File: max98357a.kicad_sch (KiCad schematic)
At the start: 1 part, among them U6 MAX98357A

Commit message: ESP32S3 branch initial changes
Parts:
- added C28: 100nf, Capacitor_SMD:C_0805_2012Metric, symbol Device:C
- added C30: 22p, Capacitor_SMD:C_0805_2012Metric, symbol Device:C
- added C37: 220p, Capacitor_SMD:C_0805_2012Metric, symbol Device:C
- added C38: 10uf, Capacitor_SMD:C_0805_2012Metric, symbol Device:C
- added L1, L3: ferrite, symbol Device:L
- added L4, L5: ferrite, Inductor_SMD:L_0805_2012Metric, symbol Device:L
- added LS1: Speaker, symbol Device:Speaker
- added R36: 1M, Resistor_SMD:R_0805_2012Metric, symbol Device:R
- added R37: 0, Jumper:SolderJumper-2_P1.3mm_Open_RoundedPad1.0x1.5mm, symbol Device:R
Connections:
- net DIN: now reaches U6.1 (DIN)
- net OUTN: now reaches U6.10 (OUTN)
- net OUTN: now also L1.1
- net GNDA: now reaches U6.11 (GND), U6.15 (GND), U6.3 (GND)
- net GNDA: now also C28.1, C30.1, C37.1, C38.1, R37.1
- net LRC: now reaches U6.14 (LRCLK)
- net BCLK: now reaches U6.16 (BCLK)
- net pad: now reaches U6.17 (PAD)
- net GAIN: now reaches U6.2 (GAIN_SLOT)
- net SD: now reaches U6.4 (~{SD_MODE})
- net SD: now also R36.2
- net at U6.7 (VDD), U6.8 (VDD): now also C28.2, C38.2, L4.1, L5.1
- net OUTP: now reaches U6.9 (OUTP)
- net OUTP: now also L3.1
- new net: C30.2, L3.2, LS1.1
- new net: C37.2, L1.2, LS1.2
- new net +3V3: L4.2, R36.1
- new net +5V: L5.2
- new net GND: R37.2

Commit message: Update KiCad project files
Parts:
- added J7: Conn_01x07_Pin, Connector_PinHeader_2.54mm:PinHeader_1x07_P2.54mm_Vertical, symbol Connector:Conn_01x07_Pin
- LS1: footprint (none) -> Connector_Molex:Molex_Micro-Latch_53253-0270_1x02_P2.00mm_Vertical
- renumbered C28 to C20, C38 to C21, C37 to C22, C30 to C23, L4 to L3, L5 to L4, L1 to L5, L3 to L6, R36 to R25, R37 to R26, U6 to U5
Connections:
- net BCLK: now also J7.5 (Pin_5)
- net DIN: now also J7.6 (Pin_6)
- net GAIN: now also J7.1 (Pin_1)
- net GNDA: now also J7.7 (Pin_7)
- net LRC: now also J7.4 (Pin_4)
- net SD: now also J7.2 (Pin_2)
- net at C20.2, C21.2, L3.1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: now also J7.3 (Pin_3)
- net pad renamed PAD
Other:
- moved on the sheet: C22, L5, L6

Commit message: Remove unused schematic files, lock files, and backup directories
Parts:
- removed R26: 0, Jumper:SolderJumper-2_P1.3mm_Open_RoundedPad1.0x1.5mm, symbol Device:R
- added JP7: 0, Jumper:SolderJumper-2_P1.3mm_Open_RoundedPad1.0x1.5mm, symbol Jumper:Jumper_2_Open
- J7: value Conn_01x07_Pin -> (none)
- L5, L6: footprint (none) -> Inductor_SMD:L_0805_2012Metric
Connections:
- net BCLK: now also J7.2 (Pin_2); no longer J7.5 (Pin_5)
- net DIN: now also J7.3 (Pin_3); no longer J7.6 (Pin_6)
- net GAIN: now also J7.4 (Pin_4); no longer J7.1 (Pin_1)
- net GND: now also JP7.1 (A)
- net GNDA: now also J7.6 (Pin_6), JP7.2 (B); no longer J7.7 (Pin_7)
- net LRC: now also J7.1 (Pin_1); no longer J7.4 (Pin_4)
- net SD: now also J7.5 (Pin_5); no longer J7.2 (Pin_2)
- net VCC_MAC98357: now reaches C20.2, C21.2, L3.1, L4.1, U5.7 (VDD), U5.8 (VDD)
- net VCC_MAC98357: now also J7.7 (Pin_7); no longer J7.3 (Pin_3)
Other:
- moved on the sheet: J7, R25

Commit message: Update all schematic files and project
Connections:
- net VCC_MAC98357 renamed VCC_MAX98357
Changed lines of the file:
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@@
 		)
 	)
-	(label "VCC_MAC98357"
+	(label "VCC_MAX98357"
 		(at 148.59 86.36 0)
 		(effects
@@
 		)
 	)
-	(label "VCC_MAC98357"
+	(label "VCC_MAX98357"
 		(at 90.17 109.22 0)
 		(effects

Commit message: Update all schematic files and project
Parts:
- added R65, R66: 100k, Resistor_SMD:R_0805_2012Metric, symbol Device:R
- added R67: 68k, Resistor_SMD:R_0805_2012Metric, symbol Device:R
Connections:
- net PAD is gone; now on net GNDA: U5.17 (PAD)
- net GAIN: now also R65.1, R66.2
- net GNDA: now also R65.2
- net SD: now also R67.1; no longer U5.4 (~{SD_MODE})
- net VCC_MAX98357: now also R66.1
- new net: R67.2, U5.4 (~{SD_MODE})
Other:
- moved on the sheet: J7

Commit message: Update schematics, PCB, and project files
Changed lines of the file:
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@@
+	)
+	(junction
+		(at 160.02 85.09)
+		(diameter 0)
+		(color 0 0 0 0)
 	)
 	(junction
@@
 	(wire
 		(pts
+			(xy 76.2 80.01) (xy 76.2 82.55)
+		)
+		(stroke
+			(width 0)
+			(type default)
+		)
+	)
+	(wire
+		(pts
 			(xy 59.69 95.25) (xy 68.58 95.25)
 		)
@@
 	(wire
 		(pts
+			(xy 116.84 101.6) (xy 119.38 101.6)
+		)
+		(stroke
+			(width 0)
+			(type default)
+		)
+	)
+	(wire
+		(pts
+			(xy 160.02 76.2) (xy 160.02 85.09)
+		)
+		(stroke
+			(width 0)
+			(type default)
+		)
+	)
+	(wire
+		(pts
 			(xy 147.32 114.3) (xy 152.4 114.3)
 		)
@@
 	(wire
 		(pts
+			(xy 160.02 86.36) (xy 173.99 86.36)
+		)
+		(stroke
+			(width 0)
+			(type default)
+		)
+	)
+	(wire
+		(pts
 			(xy 142.24 116.84) (xy 142.24 111.76)
 		)
@@
 	(wire
 		(pts
+			(xy 160.02 86.36) (xy 160.02 85.09)
+		)
+		(stroke
+			(width 0)
+			(type default)
+		)
+	)
+	(wire
+		(pts
 			(xy 218.44 106.68) (xy 218.44 113.03)
 		)
@@
 	(wire
 		(pts
-			(xy 81.28 90.17) (xy 76.2 90.17)
-		)
-		(stroke
-			(width 0)
-			(type default)
-		)
-	)
-	(wire
-		(pts
 			(xy 118.11 91.44) (xy 132.08 91.44)
 		)
@@
 	(wire
 		(pts
-			(xy 144.78 86.36) (xy 173.99 86.36)
+			(xy 144.78 85.09) (xy 160.02 85.09)
 		)
 		(stroke
@@
 	(wire
 		(pts
-			(xy 118.11 101.6) (xy 119.38 101.6)
+			(xy 144.78 85.09) (xy 144.78 86.36)
 		)
 		(stroke
@@
 	(wire
 		(pts
-			(xy 76.2 78.74) (xy 76.2 82.55)
-		)
-		(stroke
-			(width 0)
-			(type default)
-		)
-	)
-	(wire
-		(pts
 			(xy 217.17 106.68) (xy 218.44 106.68)
 		)
@@
 		(pts
 			(xy 76.2 100.33) (xy 76.2 102.87)
+		)
+		(stroke
+			(width 0)
+			(type default)
+		)
+	)
+	(wire
+		(pts
+			(xy 82.55 80.01) (xy 76.2 80.01)
+		)
+		(stroke
+			(width 0)
+			(type default)
+		)
+	)
+	(wire
+		(pts
+			(xy 88.9 90.17) (xy 76.2 90.17)
 		)
 		(stroke
@@
 	)
 	(label "VCC_MAX98357"
-		(at 148.59 86.36 0)
-		(effects
-			(font
-				(size 1.27 1.27)
-			)
-			(justify left bottom)
-		)
-	)
-	(label "VCC_MAX98357"
 		(at 59.69 104.14 0)
 		(effects
@@
 		)
 	)
-	(label "VCC_MAX98357"
-		(at 76.2 78.74 0)
-		(effects
-			(font
-				(size 1.27 1.27)
-			)
-			(justify left bottom)
+	(global_label "VCC_MAX98357"
+		(shape input)
+		(at 82.55 80.01 0)
+		(fields_autoplaced yes)
+		(effects
+			(font
+				(size 1.27 1.27)
+			)
+			(justify left)
+		)
+		(property "Intersheetrefs" "${INTERSHEET_REFS}"
+			(at 99.9284 80.01 0)
+			(hide yes)
+			(show_name no)
+			(do_not_autoplace no)
+			(effects
+				(font
+					(size 1.27 1.27)
+				)
+				(justify left)
+			)
+		)
+	)
+	(global_label "GAIN"
+		(shape input)
+		(at 118.11 104.14 180)
+		(fields_autoplaced yes)
+		(effects
+			(font
+				(size 1.27 1.27)
+			)
+			(justify right)
+		)
+		(property "Intersheetrefs" "${INTERSHEET_REFS}"
+			(at 110.8309 104.14 0)
+			(hide yes)
+			(show_name no)
+			(do_not_autoplace no)
+			(effects
+				(font
+					(size 1.27 1.27)
+				)
+				(justify right)
+			)
+		)
+	)
+	(global_label "VCC_MAX98357"
+		(shape input)
+		(at 160.02 76.2 180)
+		(fields_autoplaced yes)
+		(effects
+			(font
+				(size 1.27 1.27)
+			)
+			(justify right)
+		)
+		(property "Intersheetrefs" "${INTERSHEET_REFS}"
+			(at 142.6416 76.2 0)
+			(hide yes)
+			(show_name no)
+			(do_not_autoplace no)
+			(effects
+				(font
+					(size 1.27 1.27)
+				)
+				(justify right)
+			)
+		)
+	)
+	(global_label "SD"
+		(shape input)
+		(at 74.93 139.7 180)
+		(fields_autoplaced yes)
+		(effects
+			(font
+				(size 1.27 1.27)
+			)
+			(justify right)
+		)
+		(property "Intersheetrefs" "${INTERSHEET_REFS}"
+			(at 69.4653 139.7 0)
+			(hide yes)
+			(show_name no)
+			(do_not_autoplace no)
+			(effects
+				(font
+					(size 1.27 1.27)
+				)
+				(justify right)
+			)
+		)
+	)
+	(global_label "SD"
+		(shape input)
+		(at 59.69 92.71 0)
+		(fields_autoplaced yes)
+		(effects
+			(font
+				(size 1.27 1.27)
+			)
+			(justify left)
+		)
+		(property "Intersheetrefs" "${INTERSHEET_REFS}"
+			(at 65.1547 92.71 0)
+			(hide yes)
+			(show_name no)
+			(do_not_autoplace no)
+			(effects
+				(font
+					(size 1.27 1.27)
+				)
+				(justify left)
+			)
+		)
+	)
+	(global_label "GAIN"
+		(shape input)
+		(at 88.9 90.17 0)
+		(fields_autoplaced yes)
+		(effects
+			(font
+				(size 1.27 1.27)
+			)
+			(justify left)
+		)
+		(property "Intersheetrefs" "${INTERSHEET_REFS}"
+			(at 96.1791 90.17 0)
+			(hide yes)
+			(show_name no)
+			(do_not_autoplace no)
+			(effects
+				(font
+					(size 1.27 1.27)
+				)
+				(justify left)
+			)
+		)
+	)
+	(global_label "SD"
+		(shape input)
+		(at 116.84 101.6 180)
+		(fields_autoplaced yes)
+		(effects
+			(font
+				(size 1.27 1.27)
+			)
+			(justify right)
+		)
+		(property "Intersheetrefs" "${INTERSHEET_REFS}"
+			(at 111.3753 101.6 0)
+			(hide yes)
+			(show_name no)
+			(do_not_autoplace no)
+			(effects
+				(font
+					(size 1.27 1.27)
+				)
+				(justify right)
+			)
 		)
 	)
@@
 		)
 	)
-	(hierarchical_label "GAIN"
-		(shape input)
-		(at 81.28 90.17 0)
-		(effects
-			(font
-				(size 1.27 1.27)
-			)
-			(justify left)
-		)
-	)
-	(hierarchical_label "GAIN"
-		(shape input)
-		(at 118.11 104.14 180)
+	(hierarchical_label "BCLK"
+		(shape input)
+		(at 118.11 93.98 180)
 		(effects
 			(font
@@
 		)
 	)
-	(hierarchical_label "SD"
-		(shape input)
-		(at 59.69 92.71 0)
-		(effects
-			(font
-				(size 1.27 1.27)
-			)
-			(justify left)
-		)
-	)
-	(hierarchical_label "BCLK"
-		(shape input)
-		(at 118.11 93.98 180)
-		(effects
-			(font
-				(size 1.27 1.27)
-			)
-			(justify right)
-		)
-	)
-	(hierarchical_label "SD"
-		(shape input)
-		(at 118.11 101.6 180)
-		(effects
-			(font
-				(size 1.27 1.27)
-			)
-			(justify right)
-		)
-	)
 	(hierarchical_label "DIN"
 		(shape input)
@@
 		(effects
 			(font
-				(size 1.27 1.27)
-			)
-			(justify right)
-		)
-	)
-	(hierarchical_label "SD"
-		(shape input)
-		(at 74.93 139.7 180)
-		(effects
-			(font

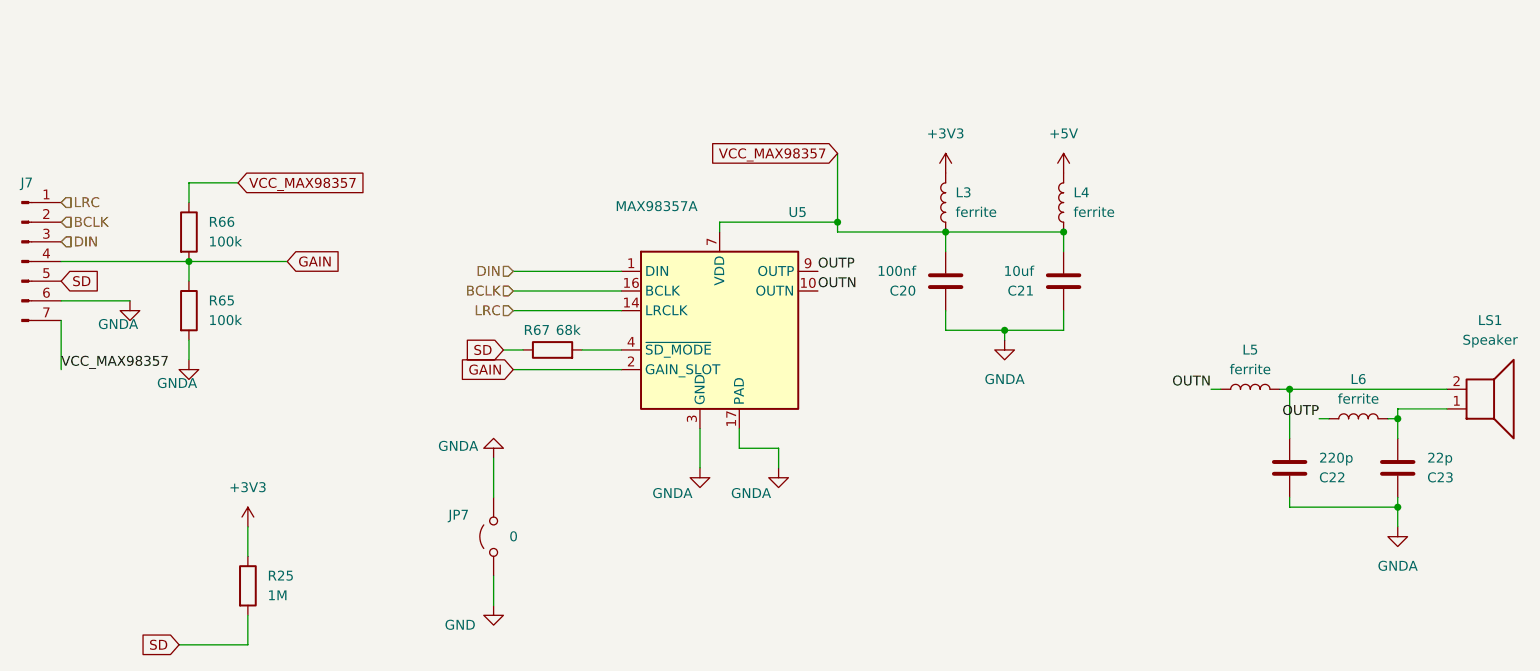
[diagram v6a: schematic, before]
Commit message: Actualización de esquema y PCB del proyecto ESP32C6 Xiaozhi
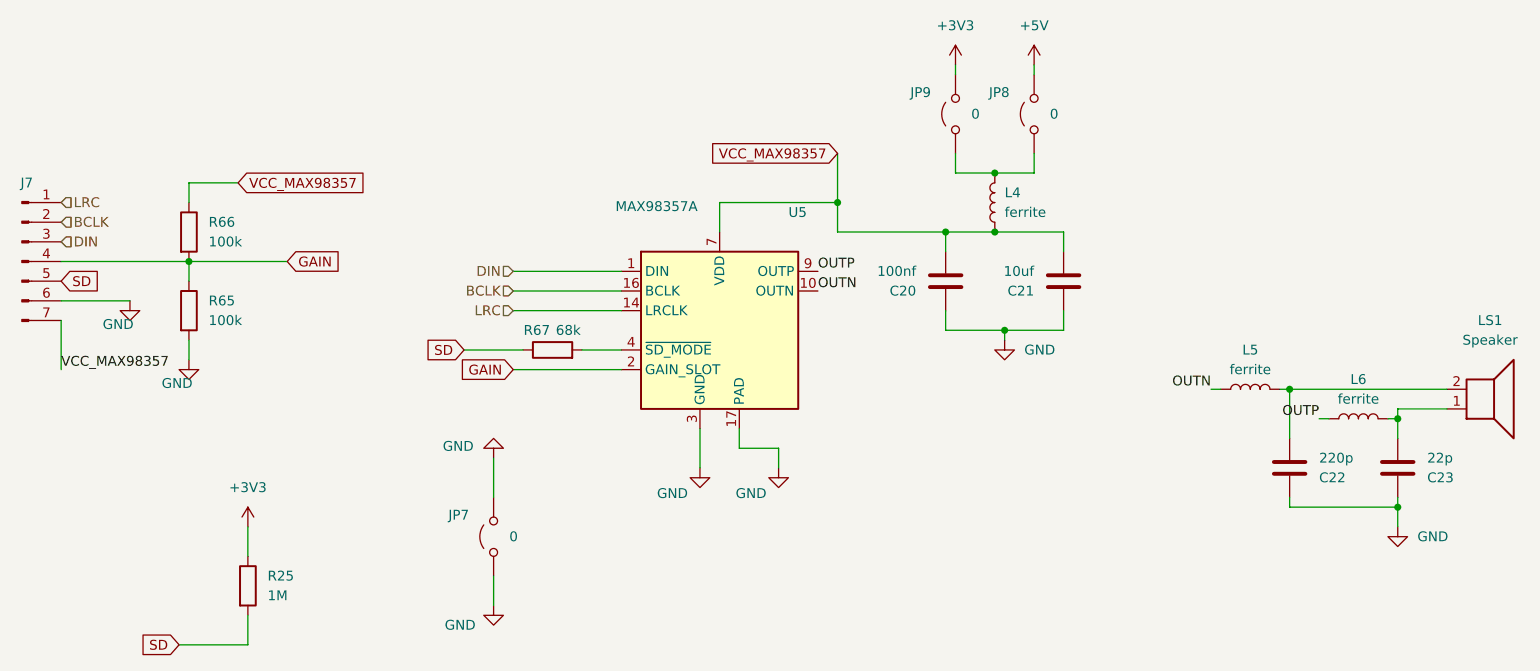
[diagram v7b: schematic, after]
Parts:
- removed L3: ferrite, Inductor_SMD:L_0805_2012Metric, symbol Device:L
- added JP8, JP9: 0, Jumper:SolderJumper-2_P1.3mm_Open_RoundedPad1.0x1.5mm, symbol Jumper:Jumper_2_Open
- JP7: footprint Jumper:SolderJumper-2_P1.3mm_Open_RoundedPad1.0x1.5mm -> Jumper:SolderJumper-2_P1.3mm_Bridged_RoundedPad1.0x1.5mm
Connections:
- net GNDA is gone; now on net GND: C20.1, C21.1, C22.1, C23.1, J7.6 (Pin_6), JP7.2 (B), R65.2, U5.11 (GND), U5.15 (GND), U5.17 (PAD), U5.3 (GND)
- net +3V3: now also JP9.2 (B)
- net +5V: now also JP8.2 (B); no longer L4.2
- new net: JP8.1 (A), JP9.1 (A), L4.2
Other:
- moved on the sheet: L4

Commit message: Update KiCad schematics/PCB and project files
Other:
- moved on the sheet: R66
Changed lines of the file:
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@@
 	(wire
 		(pts
-			(xy 76.2 80.01) (xy 76.2 82.55)
+			(xy 76.2 80.01) (xy 76.2 81.28)
 		)
 		(stroke
@@
 		(pts
 			(xy 144.78 82.55) (xy 144.78 86.36)
+		)
+		(stroke
+			(width 0)
+			(type default)
+		)
+	)
+	(wire
+		(pts
+			(xy 76.2 88.9) (xy 76.2 90.17)
 		)
 		(stroke
@@
 	(symbol
 		(lib_id "Device:R")
-		(at 76.2 86.36 0)
+		(at 76.2 85.09 0)
 		(unit 1)
 		(body_style 1)
@@
 		(fields_autoplaced yes)
 		(property "Reference" "R66"
-			(at 78.74 85.0899 0)
+			(at 78.74 83.8199 0)
 			(show_name no)
 			(do_not_autoplace no)
@@
 		)
 		(property "Value" "100k"
-			(at 78.74 87.6299 0)
+			(at 78.74 86.3599 0)
 			(show_name no)
 			(do_not_autoplace no)
@@
 		)
 		(property "Footprint" "Resistor_SMD:R_0805_2012Metric"
-			(at 74.422 86.36 90)
+			(at 74.422 85.09 90)
 			(hide yes)
 			(show_name no)
@@
 		)
 		(property "Datasheet" ""
-			(at 76.2 86.36 0)
+			(at 76.2 85.09 0)
 			(hide yes)
 			(show_name no)
@@
 		)
 		(property "Description" ""
-			(at 76.2 86.36 0)
-			(show_name no)
-			(do_not_autoplace no)
+			(at 76.2 85.09 0)
+			(show_name no)
+			(do_not_autoplace no)
